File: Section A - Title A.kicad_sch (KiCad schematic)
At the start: 25 parts, among them J1 10155435-00011LF, J3 691382010012, U1 ESP32-S3-WROOM-2, U6 DS3231MZ

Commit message: Finished most routing, final checks to be done
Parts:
- removed J3: 691382010012, 691382010012:691382010012, symbol 691382010012:691382010012
- added BT1: Battery_Cell, Battery:BatteryHolder_MYOUNG_BS-07-A1BJ001_CR2032, symbol Device:Battery_Cell
- added J3, J7: 691382010006, 691382010006:691382010006, symbol 691382010006:691382010006
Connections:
- net SDA is gone; now on net I2C_SDA: R10.2, U6.7 (SDA)
- net +3V0: now also BT1.1 (+)
- net +5V: now also J3.1, J7.1
- net CAN2_INT: now also U1.25 (IO48); no longer U1.17 (IO9)
- net GND: now also BT1.2 (-), J3.2, J7.2
- net I2C_SDA: now reaches U1.12 (IO8)
- net GPIO_A1: now reaches U1.35 (MTMS/IO42)
- net GPIO_A1: now also J3.3
- net GPIO_A2: now reaches U1.36 (RXD0/IO44)
- net GPIO_A2: now also J3.4
- net GPIO_A3: now reaches U1.37 (TXD0/IO43)
- net GPIO_A3: now also J3.5
- net GPIO_A4: now reaches U1.38 (IO2)
- net GPIO_A4: now also J3.6
- net GPIO_B4: now reaches U1.5 (IO5)
- net GPIO_B4: now also J7.6
- net GPIO_B3: now reaches U1.6 (IO6)
- net GPIO_B3: now also J7.5
- net GPIO_B2: now reaches U1.7 (IO7)
- net GPIO_B2: now also J7.4
- net GPIO_B1: now reaches U1.8 (IO15)
- net GPIO_B1: now also J7.3
- net SCL renamed I2C_SCL
- net I2C_SCL: now also U1.17 (IO9)
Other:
- moved on the sheet: C5, D1, R10, R9

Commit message: Final Changes, Updated to Checked
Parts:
- removed BT1: Battery_Cell, Battery:BatteryHolder_MYOUNG_BS-07-A1BJ001_CR2032, symbol Device:Battery_Cell
- removed C22, C23: 1u, Capacitor_SMD:C_0603_1608Metric_Pad1.08x0.95mm_HandSolder, symbol Device:C
- removed H1, H2, H3, H4: MountingHole_Pad, MountingHole:MountingHole_3.2mm_M3_DIN965_Pad, symbol Mechanical:MountingHole_Pad
- removed R10, R11, R9: 5.1k, Resistor_SMD:R_0603_1608Metric_Pad0.98x0.95mm_HandSolder, symbol Device:R
- removed U6: DS3231MZ, Package_SO:SOIC-8_3.9x4.9mm_P1.27mm, symbol Timer_RTC:DS3231MZ
- C1, C3: value 1u -> 1uF
- C2, C4: value 0.1u -> 0.1uF
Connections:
- no-connect marks 8 -> 14
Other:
- moved on the sheet: C1, C2, C3, C4, C5, D1, J1, J3, J7, R1, R2, R3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

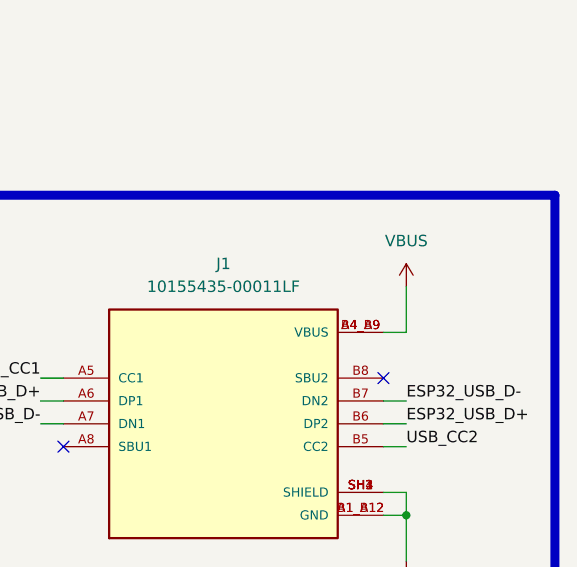
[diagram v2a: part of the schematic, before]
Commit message: Retry with rules DRC ERC passing
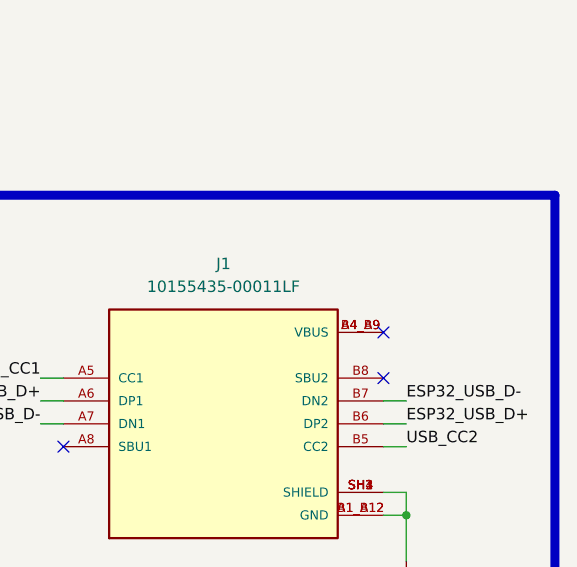
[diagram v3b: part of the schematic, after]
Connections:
- net VBUS: no longer names the net of J1.A4_B9 (VBUS), J1.B4_A9 (VBUS)
- no-connect marks 14 -> 15
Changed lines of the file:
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@@
 		(at 102.87 107.95)
 	)
+	(no_connect
+		(at 248.92 46.99)
+	)
 	(wire
 		(pts
@@
 	(wire
 		(pts
-			(xy 248.92 46.99) (xy 251.46 46.99)
-		)
-		(stroke
-			(width 0)
-			(type default)
-		)
-	)
-	(wire
-		(pts
 			(xy 168.91 73.66) (xy 177.8 73.66)
 		)
@@
 	(wire
 		(pts
-			(xy 251.46 41.91) (xy 251.46 46.99)
-		)
-		(stroke
-			(width 0)
-			(type default)
-		)
-	)
-	(wire
-		(pts
 			(xy 172.72 66.04) (xy 177.8 66.04)
 		)
@@
 					(unit 1)
 				)
-			)
-		)
-	)
-	(symbol
-		(lib_id "power:VBUS")
-		(at 251.46 41.91 0)
-		(unit 1)
-		(exclude_from_sim no)
-		(in_bom yes)
-		(on_board yes)
-		(dnp no)
-		(fields_autoplaced yes)
-		(property "Reference" "#PWR017"
-			(at 251.46 45.72 0)
-			(effects
-				(font
-					(size 1.27 1.27)
-				)
-				(hide yes)
-			)
-		)
-		(property "Value" "VBUS"
-			(at 251.46 36.83 0)
-			(effects
-				(font
-					(size 1.27 1.27)
-				)
-			)
-		)
-		(property "Footprint" ""
-			(at 251.46 41.91 0)
-			(effects
-				(font
-					(size 1.27 1.27)
-				)
-				(hide yes)
-			)
-		)
-		(property "Datasheet" ""
-			(at 251.46 41.91 0)
-			(effects
-				(font
-					(size 1.27 1.27)
-				)
-				(hide yes)
-			)
-		)
-		(property "Description" "Power symbol creates a global label with name \"VBUS\""
-			(at 251.46 41.91 0)
-			(effects
-				(font
-					(size 1.27 1.27)
-				)
-				(hide yes)
-			)
-		)
-		(pin "1"
-		)
-		(instances
-			(project ""
-				(path "/f9e05184-c88b-4a88-ae9c-ab2bdb32be7c/c5103ceb-5325-4a84-a025-9638a412984e/f06537ee-772d-44d3-8c50-e0ba41038c9c"
-					(reference "#PWR017")
-					(unit 1)
-				)

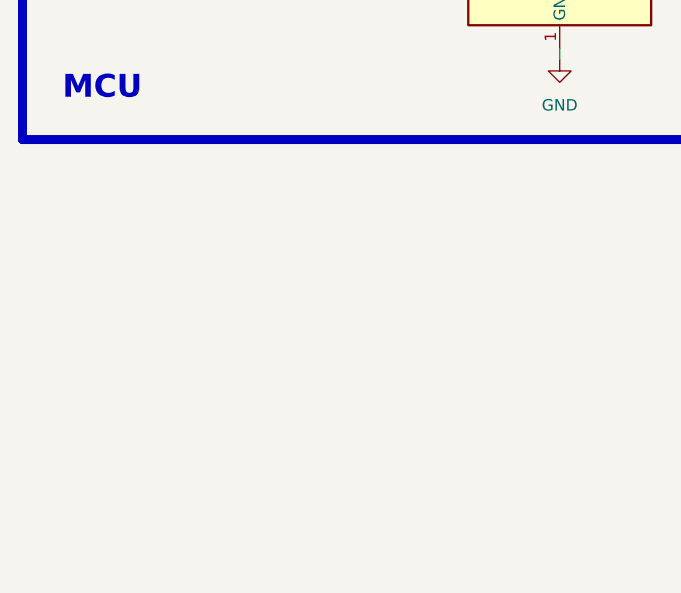
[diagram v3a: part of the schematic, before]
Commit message: Added pulldowns on GPIOs
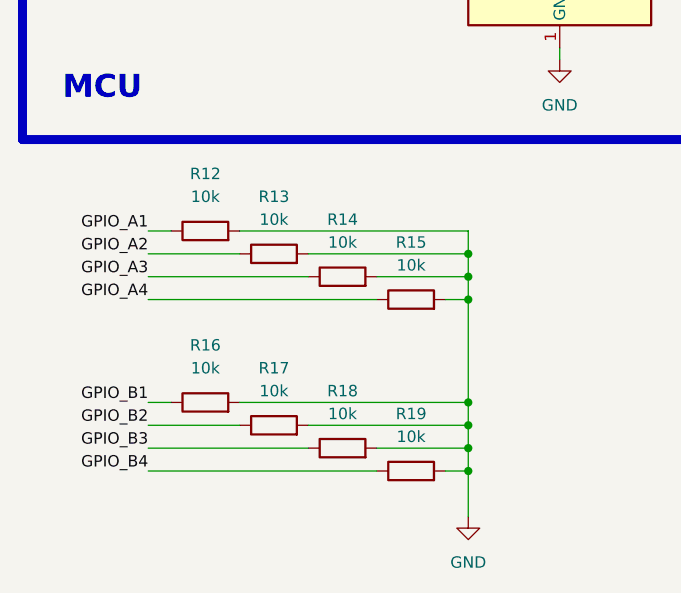
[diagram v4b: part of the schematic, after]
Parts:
- added R12, R13, R14, R15, R16, R17, R18, R19: 10k, Resistor_SMD:R_0603_1608Metric_Pad0.98x0.95mm_HandSolder, symbol Device:R
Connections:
- net GND: now also R12.2, R13.2, R14.2, R15.2, R16.2, R17.2, R18.2, R19.2
- net GPIO_A1: now also R12.1
- net GPIO_A2: now also R13.1
- net GPIO_A3: now also R14.1
- net GPIO_A4: now also R15.1
- net GPIO_B1: now also R16.1
- net GPIO_B2: now also R17.1
- net GPIO_B3: now also R18.1
- net GPIO_B4: now also R19.1
